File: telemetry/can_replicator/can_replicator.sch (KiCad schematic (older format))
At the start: 33 parts, among them J1 CONN_02X03, U1 MCP2561-E_SN, U2 ATMEGA16M1, U3 USB_MicroB, U4 FT232RL, Y1 Crystal_SMD

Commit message: feat: change to 3 debug LEDs
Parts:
- removed D?: LED_0805, footprints:LED_0805_OEM, symbol formula:LED_0805
- removed R?: R_270K, footprints:R_0805_OEM, symbol formula:R_270K
- gave numbers to parts that had none: 7
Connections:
- net labels removed: DBG4
- wire segments 75 -> 73
- no-connect marks 28 -> 29
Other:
- moved on the sheet: D4, D5, D6

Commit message: fix: change LEDs to 200ohm resistors
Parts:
- removed R4, R5, R6, R7, R8, R9: R_270K, footprints:R_0805_OEM, symbol formula:R_270K
- added R? (x6): R_200K, footprints:R_0805_OEM, symbol formula:R_200K
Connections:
- wire segments 73 -> 76
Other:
- moved on the sheet: D4, D5, D6

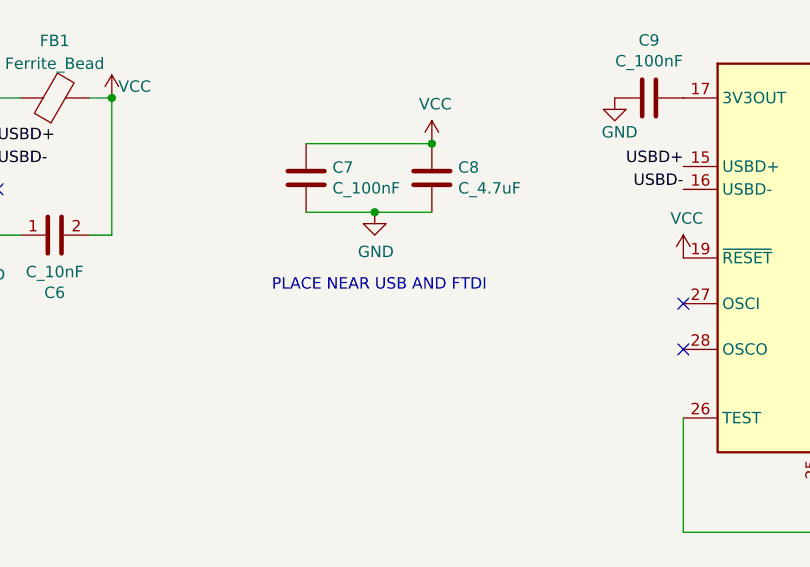
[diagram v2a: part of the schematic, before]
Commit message: docs: update placement of decoupling caps
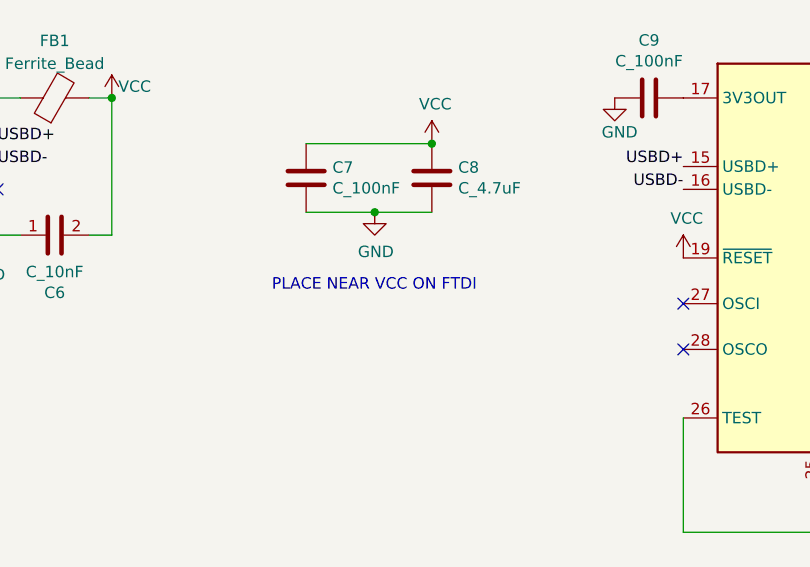
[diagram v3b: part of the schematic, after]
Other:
- note added: "PLACE NEAR VCC ON FTDI"
- note removed: "PLACE NEAR USB AND FTDI"
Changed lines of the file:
@@
 NoConn ~ 3800 1700
 Text Notes 12400 2650 0    50   ~ 0
-PLACE NEAR USB AND FTDI
+PLACE NEAR VCC ON FTDI
 $Comp
 L formula:LED_0805 D4

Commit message: chore: annotate schematic
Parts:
- gave numbers to parts that had none: 6
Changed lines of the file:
@@
 $EndComp
 $Comp
-L power:GND #PWR?
+L power:GND #PWR024
 U 1 1 5FB7CF68
 P 15900 8850
-F 0 "#PWR?" H 15900 8600 50  0001 C CNN
+F 0 "#PWR024" H 15900 8600 50  0001 C CNN
 F 1 "GND" H 15905 8677 50  0000 C CNN
 F 2 "" H 15900 8850 50  0001 C CNN
@@
 NoConn ~ 3800 1600
 $Comp
-L formula:R_200K R?
+L formula:R_200K R7
 U 1 1 5FB83E8C
 P 15750 6750
-F 0 "R?" V 15543 6750 50  0000 C CNN
+F 0 "R7" V 15543 6750 50  0000 C CNN
 F 1 "R_200K" V 15634 6750 50  0000 C CNN
 F 2 "footprints:R_0805_OEM" H 15680 6750 50  0001 C CNN
@@
 $EndComp
 $Comp
-L formula:R_200K R?
+L formula:R_200K R8
 U 1 1 5FB8465B
 P 15750 7150
-F 0 "R?" V 15543 7150 50  0000 C CNN
+F 0 "R8" V 15543 7150 50  0000 C CNN
 F 1 "R_200K" V 15634 7150 50  0000 C CNN
 F 2 "footprints:R_0805_OEM" H 15680 7150 50  0001 C CNN
@@
 $EndComp
 $Comp
-L formula:R_200K R?
+L formula:R_200K R9
 U 1 1 5FB84F88
 P 15750 7500
-F 0 "R?" V 15543 7500 50  0000 C CNN
+F 0 "R9" V 15543 7500 50  0000 C CNN
 F 1 "R_200K" V 15634 7500 50  0000 C CNN
 F 2 "footprints:R_0805_OEM" H 15680 7500 50  0001 C CNN
@@
 $EndComp
 $Comp
-L formula:R_200K R?
+L formula:R_200K R4
 U 1 1 5FB85882
 P 15700 8150
-F 0 "R?" V 15493 8150 50  0000 C CNN
+F 0 "R4" V 15493 8150 50  0000 C CNN
 F 1 "R_200K" V 15584 8150 50  0000 C CNN
 F 2 "footprints:R_0805_OEM" H 15630 8150 50  0001 C CNN
@@
 	15850 8150 15900 8150
 $Comp
-L formula:R_200K R?
+L formula:R_200K R5
 U 1 1 5FB865BA
 P 15700 8500
-F 0 "R?" V 15493 8500 50  0000 C CNN
+F 0 "R5" V 15493 8500 50  0000 C CNN
 F 1 "R_200K" V 15584 8500 50  0000 C CNN
 F 2 "footprints:R_0805_OEM" H 15630 8500 50  0001 C CNN
@@
 	15850 8500 15900 8500
 $Comp
-L formula:R_200K R?
+L formula:R_200K R6
 U 1 1 5FB86F49
 P 15700 8850
-F 0 "R?" V 15493 8850 50  0000 C CNN
+F 0 "R6" V 15493 8850 50  0000 C CNN
 F 1 "R_200K" V 15584 8850 50  0000 C CNN
 F 2 "footprints:R_0805_OEM" H 15630 8850 50  0001 C CNN

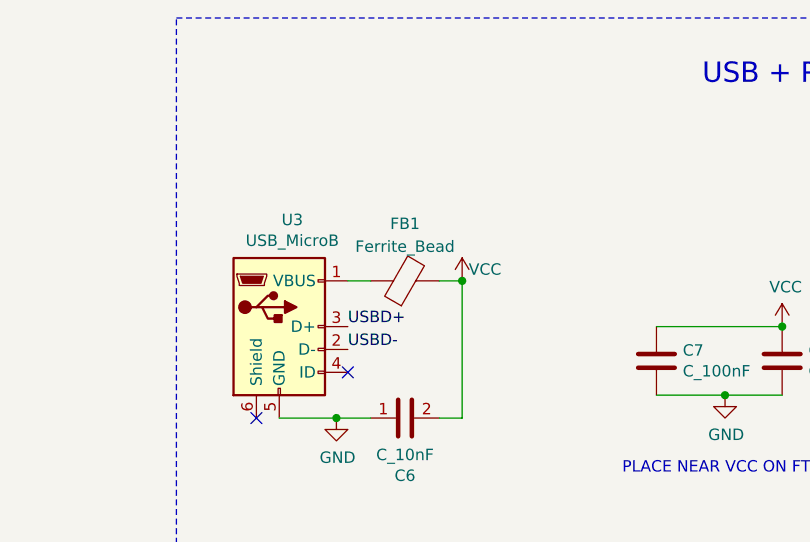
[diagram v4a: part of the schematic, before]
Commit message: feat: remove ferrite bead
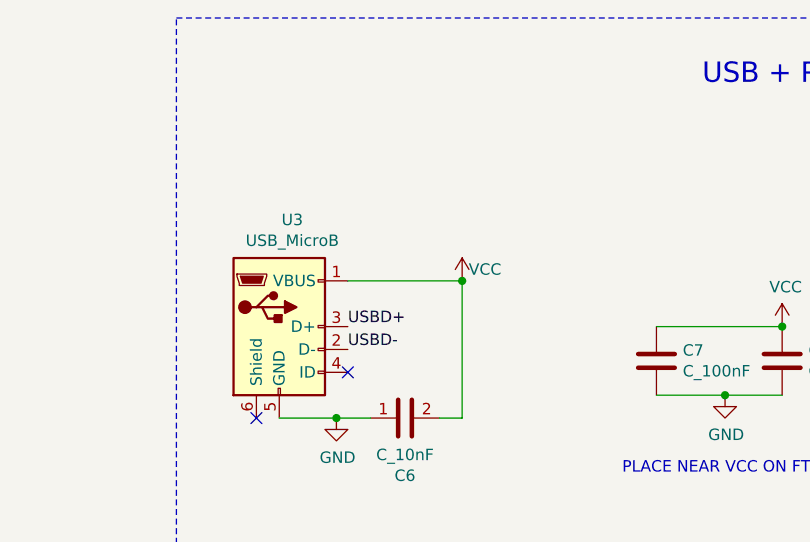
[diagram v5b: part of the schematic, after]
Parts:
- removed FB1: Ferrite_Bead, symbol Device:Ferrite_Bead
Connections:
- net VCC: now also U3.1 (VBUS)
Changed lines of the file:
@@
 Wire Wire Line
 	11300 2400 11150 2400
-Wire Wire Line
-	11200 1800 11300 1800
-$Comp
-L Device:Ferrite_Bead FB1
-U 1 1 5FAF9058
-P 11450 1800
-F 0 "FB1" V 11700 1800 50  0000 C CNN
-F 1 "Ferrite_Bead" V 11600 1800 50  0000 C CNN
-F 2 "" V 11380 1800 50  0001 C CNN
-F 3 "~" H 11450 1800 50  0001 C CNN
-	1    11450 1800
-	0    -1   -1   0
-$EndComp
-Wire Wire Line
-	11600 1800 11700 1800
 Connection ~ 11700 1800
 $Comp
@@
 Wire Wire Line
 	15850 8850 15900 8850
+Wire Wire Line
+	11200 1800 11700 1800
 $EndSCHEMATC

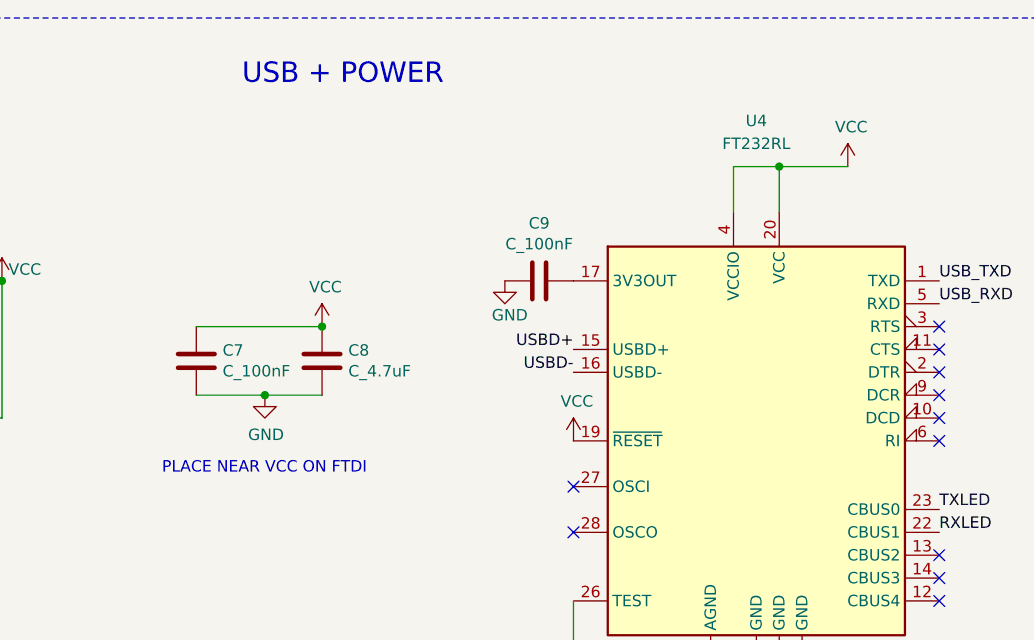
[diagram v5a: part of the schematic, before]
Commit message: style: move decoupling caps near FTDI
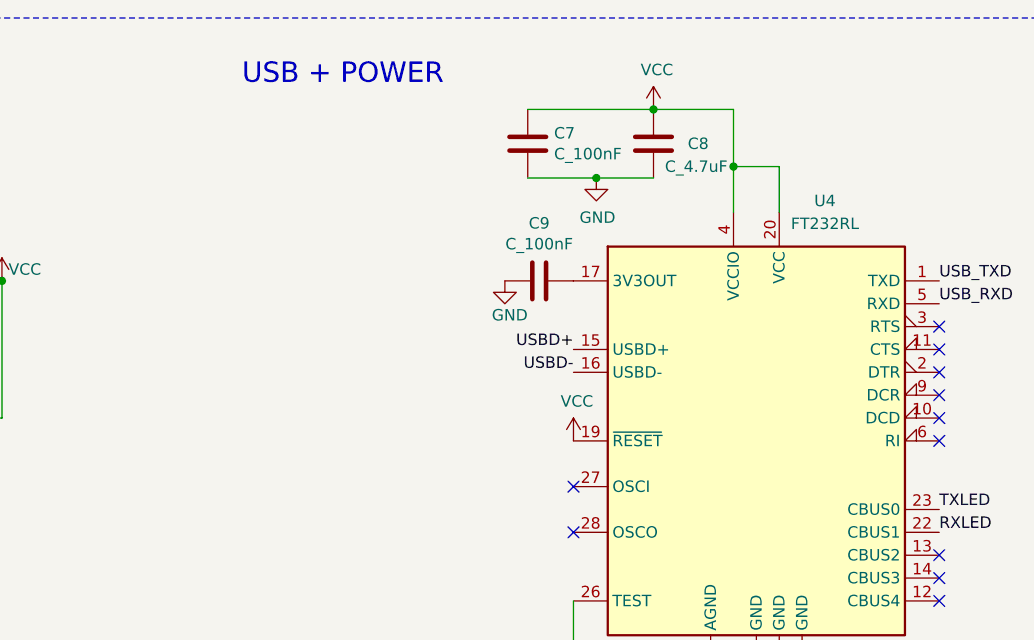
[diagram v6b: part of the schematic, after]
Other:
- note removed: "PLACE NEAR VCC ON FTDI"
- moved on the sheet: C7, C8
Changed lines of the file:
@@
 U 1 1 5FA978AD
 P 15000 2500
-F 0 "U4" H 15000 3900 50  0000 C CNN
-F 1 "FT232RL" H 15000 3800 50  0000 C CNN
+F 0 "U4" H 15300 3550 50  0000 C CNN
+F 1 "FT232RL" H 15300 3450 50  0000 C CNN
 F 2 "Package_SO:SSOP-28_5.3x10.2mm_P0.65mm" H 16100 1600 50  0001 C CNN
 F 3 "https://www.ftdichip.com/Support/Documents/DataSheets/ICs/DS_FT232R.pdf" H 15000 2500 50  0001 C CNN
@@
 Wire Wire Line
 	15100 1500 15100 1300
-Connection ~ 15100 1300
-Wire Wire Line
-	15100 1300 15400 1300
-$Comp
-L power:VCC #PWR0103
-U 1 1 5FADCCAF
-P 15400 1300
-F 0 "#PWR0103" H 15400 1150 50  0001 C CNN
-F 1 "VCC" H 15415 1473 50  0000 C CNN
-F 2 "" H 15400 1300 50  0001 C CNN
-F 3 "" H 15400 1300 50  0001 C CNN
-	1    15400 1300
-	1    0    0    -1
-$EndComp
 Connection ~ 11150 2400
 $Comp
@@
 L power:GND #PWR0107
 U 1 1 5FB2AA73
-P 12850 2300
-F 0 "#PWR0107" H 12850 2050 50  0001 C CNN
-F 1 "GND" H 12855 2127 50  0000 C CNN
-F 2 "" H 12850 2300 50  0001 C CNN
-F 3 "" H 12850 2300 50  0001 C CNN
-	1    12850 2300
-	1    0    0    -1
-$EndComp
-Connection ~ 12850 2300
-Wire Wire Line
-	12850 2300 13100 2300
+P 14300 1350
+F 0 "#PWR0107" H 14300 1100 50  0001 C CNN
+F 1 "GND" H 14305 1177 50  0000 C CNN
+F 2 "" H 14300 1350 50  0001 C CNN
+F 3 "" H 14300 1350 50  0001 C CNN
+	1    14300 1350
+	1    0    0    -1
+$EndComp
+Connection ~ 14300 1350
+Wire Wire Line
+	14300 1350 14550 1350
 $Comp
 L formula:C_100nF C7
 U 1 1 5FB2B96B
-P 12550 2150
-F 0 "C7" H 12665 2196 50  0000 L CNN
-F 1 "C_100nF" H 12665 2105 50  0000 L CNN
-F 2 "footprints:C_0603_1608Metric" H 12588 2000 50  0001 C CNN
-F 3 "http://www.samsungsem.com/kr/support/product-search/mlcc/CL10A475KQ8NNNC.jsp" H 12575 2250 50  0001 C CNN
-F 4 "DK" H 12550 2150 60  0001 C CNN "MFN"
-F 5 "1276-6717-1-ND" H 12550 2150 60  0001 C CNN "MPN"
-F 6 "https://www.digikey.com/product-detail/en/samsung-electro-mechanics/CL10B104KA8WPNC/1276-6717-1-ND/5961576" H 12975 2650 60  0001 C CNN "PurchasingLink"
-	1    12550 2150
-	1    0    0    -1
-$EndComp
-Wire Wire Line
-	12550 2000 13100 2000
+P 14000 1200
+F 0 "C7" H 14115 1246 50  0000 L CNN
+F 1 "C_100nF" H 14115 1155 50  0000 L CNN
+F 2 "footprints:C_0603_1608Metric" H 14038 1050 50  0001 C CNN
+F 3 "http://www.samsungsem.com/kr/support/product-search/mlcc/CL10A475KQ8NNNC.jsp" H 14025 1300 50  0001 C CNN
+F 4 "DK" H 14000 1200 60  0001 C CNN "MFN"
+F 5 "1276-6717-1-ND" H 14000 1200 60  0001 C CNN "MPN"
+F 6 "https://www.digikey.com/product-detail/en/samsung-electro-mechanics/CL10B104KA8WPNC/1276-6717-1-ND/5961576" H 14425 1700 60  0001 C CNN "PurchasingLink"
+	1    14000 1200
+	1    0    0    -1
+$EndComp
+Wire Wire Line
+	14000 1050 14550 1050
 $Comp
 L formula:C_4.7uF C8
 U 1 1 5FB2C8CC
-P 13100 2150
-F 0 "C8" H 13215 2196 50  0000 L CNN
-F 1 "C_4.7uF" H 13215 2105 50  0000 L CNN
-F 2 "footprints:C_0603_1608Metric" H 13138 2000 50  0001 C CNN
-F 3 "http://www.samsungsem.com/kr/support/product-search/mlcc/CL10A475KQ8NNNC.jsp" H 13125 2250 50  0001 C CNN
-F 4 "DK" H 13100 2150 60  0001 C CNN "MFN"
-F 5 "1276-1045-1-ND" H 13100 2150 60  0001 C CNN "MPN"
-F 6 "https://www.digikey.com/product-detail/en/samsung-electro-mechanics/CL10A475KQ8NNNC/1276-1045-1-ND/3889131" H 13525 2650 60  0001 C CNN "PurchasingLink"
-	1    13100 2150
-	1    0    0    -1
-$EndComp
-Wire Wire Line
-	12550 2300 12850 2300
+P 14550 1200
+F 0 "C8" H 14700 1200 50  0000 L CNN
+F 1 "C_4.7uF" H 14600 1100 50  0000 L CNN
+F 2 "footprints:C_0603_1608Metric" H 14588 1050 50  0001 C CNN
+F 3 "http://www.samsungsem.com/kr/support/product-search/mlcc/CL10A475KQ8NNNC.jsp" H 14575 1300 50  0001 C CNN
+F 4 "DK" H 14550 1200 60  0001 C CNN "MFN"
+F 5 "1276-1045-1-ND" H 14550 1200 60  0001 C CNN "MPN"
+F 6 "https://www.digikey.com/product-detail/en/samsung-electro-mechanics/CL10A475KQ8NNNC/1276-1045-1-ND/3889131" H 14975 1700 60  0001 C CNN "PurchasingLink"
+	1    14550 1200
+	1    0    0    -1
+$EndComp
+Wire Wire Line
+	14000 1350 14300 1350
 $Comp
 L formula:LED_0805 D3
@@
 L power:VCC #PWR020
 U 1 1 5FB37814
-P 13100 2000
-F 0 "#PWR020" H 13100 1850 50  0001 C CNN
-F 1 "VCC" H 13115 2173 50  0000 C CNN
-F 2 "" H 13100 2000 50  0001 C CNN
-F 3 "" H 13100 2000 50  0001 C CNN
-	1    13100 2000
-	1    0    0    -1
-$EndComp
-Connection ~ 13100 2000
+P 14550 1050
+F 0 "#PWR020" H 14550 900 50  0001 C CNN
+F 1 "VCC" H 14565 1223 50  0000 C CNN
+F 2 "" H 14550 1050 50  0001 C CNN
+F 3 "" H 14550 1050 50  0001 C CNN
+	1    14550 1050
+	1    0    0    -1
+$EndComp
+Connection ~ 14550 1050
 $Comp
 L power:GND #PWR023
@@
 NoConn ~ 3800 2000
 NoConn ~ 3800 1700
-Text Notes 12400 2650 0    50   ~ 0
-PLACE NEAR VCC ON FTDI
 $Comp
 L formula:LED_0805 D4
@@
 Wire Wire Line
 	11200 1800 11700 1800
+Wire Wire Line
+	14550 1050 14900 1050
+Wire Wire Line
+	14900 1050 14900 1300
+Connection ~ 14900 1300
 $EndSCHEMATC

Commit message: fix: misc. fixes based on design checklist
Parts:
- removed R4, R5, R6, R7, R8, R9: R_200K, footprints:R_0805_OEM, symbol formula:R_200K
- added J2: MM_M_VT_20, footprints:micromatch_female_vert_20, symbol formula:MM_M_VT_20
- added R4, R5, R6, R7, R8, R9: R_200, footprints:R_0805_OEM, symbol formula:R_200
- added TP1, TP2: TP, footprints:tp_1.6mm, symbol formula:TP
- U3: footprint Connectors_USB:USB_Micro-B_Molex-105017-0001 -> Connector_USB:USB_Micro-B_Molex-105017-0001
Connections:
- net GND: now also J2.1, J2.10, J2.11, J2.12, J2.13, J2.14, J2.15, J2.16, J2.17, J2.18, J2.19, J2.20, J2.5, J2.6, J2.7, J2.8, J2.9, R4.1, R5.1, R6.1, R9.1, TP1.1 (TP)
- net RXLED: now also R7.1
- net TXLED: now also R8.1
- net VCC: now also TP2.1 (TP)
- net at D3.1 (K): now also R9.2
- net at D4.1 (K): now also R4.2
- net at D2.1 (K): now also R8.2
- net at D1.1 (K): now also R7.2
- net at D5.1 (K): now also R5.2
- net at D6.1 (K): now also R6.2
- net CAN_HI renamed CAN_+
- net CAN_+: now also J2.3
- net CAN_LO renamed CAN_-
- net CAN_-: now also J2.4
- no-connect marks 29 -> 30
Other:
- moved on the sheet: C1, C2, C3, C4, C5, C6, C7, C8, C9, D1, D2, D3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

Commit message: fix: begin removal of template-rescue
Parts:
- added D?: D_Zener_5.6V, footprints:D_5.6V_Zener, symbol formula:D_Zener_5.6V
- U2: symbol template-rescue:ATMEGA16M1-formula -> formula:ATMEGA16M1
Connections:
- net GND: now also D?.2 (A)
- net VCC: now also D?.1 (K)
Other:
- note removed: "POWER FLAGS\n"
- moved on the sheet: C6
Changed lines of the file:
@@
 Comment4 ""
 $EndDescr
-$Comp
-L power:GND #PWR0108
-U 1 1 5BEE3CCE
-P 15300 2800
-F 0 "#PWR0108" H 15300 2550 50  0001 C CNN
-F 1 "GND" H 15305 2627 50  0000 C CNN
-F 2 "" H 15300 2800 50  0001 C CNN
-F 3 "" H 15300 2800 50  0001 C CNN
-	1    15300 2800
-	1    0    0    -1
-$EndComp
 Text Label 3950 2550 0    50   ~ 0
 CAN_TX
@@
 Text Notes 3850 5350 0    89   ~ 0
 16 MHz CRYSTAL\n
-Text Notes 14900 2350 0    89   ~ 0
-POWER FLAGS\n
-$Comp
-L power:PWR_FLAG #FLG02
-U 1 1 5D615167
-P 14900 2650
-F 0 "#FLG02" H 14900 2725 50  0001 C CNN
-F 1 "PWR_FLAG" H 14900 2824 50  0000 C CNN
-F 2 "" H 14900 2650 50  0001 C CNN
-F 3 "~" H 14900 2650 50  0001 C CNN
-	1    14900 2650
-	1    0    0    -1
-$EndComp
-$Comp
-L power:PWR_FLAG #FLG03
-U 1 1 5D615217
-P 15300 2650
-F 0 "#FLG03" H 15300 2725 50  0001 C CNN
-F 1 "PWR_FLAG" H 15300 2824 50  0000 C CNN
-F 2 "" H 15300 2650 50  0001 C CNN
-F 3 "~" H 15300 2650 50  0001 C CNN
-	1    15300 2650
-	1    0    0    -1
-$EndComp
-$Comp
-L power:VCC #PWR016
-U 1 1 5D6181B6
-P 14900 2800
-F 0 "#PWR016" H 14900 2650 50  0001 C CNN
-F 1 "VCC" H 14918 2973 50  0000 C CNN
-F 2 "" H 14900 2800 50  0001 C CNN
-F 3 "" H 14900 2800 50  0001 C CNN
-	1    14900 2800
-	-1   0    0    1
-$EndComp
-$Comp
-L power:GND #PWR017
-U 1 1 5D622997
-P 15600 2800
-F 0 "#PWR017" H 15600 2550 50  0001 C CNN
-F 1 "GND" H 15605 2627 50  0000 C CNN
-F 2 "" H 15600 2800 50  0001 C CNN
-F 3 "" H 15600 2800 50  0001 C CNN
-	1    15600 2800
-	1    0    0    -1
-$EndComp
-Text Label 15600 2650 2    50   ~ 0
-GND
 $Comp
 L template-rescue:CONN_02X03-formula J1
@@
 Wire Wire Line
 	6950 2400 6950 2450
-Wire Wire Line
-	14900 2650 14900 2800
-Wire Wire Line
-	15300 2650 15300 2800
-Wire Wire Line
-	15600 2650 15600 2800
 Wire Wire Line
 	6850 2400 6950 2400
@@
 	1    0    0    -1
 $EndComp
-Wire Wire Line
-	2000 7550 2000 6950
-Wire Wire Line
-	2000 7550 1900 7550
 $Comp
 L formula:C_10nF C6
 U 1 1 5FAF39CA
-P 1750 7550
-F 0 "C6" V 1498 7550 50  0000 C CNN
-F 1 "C_10nF" V 1589 7550 50  0000 C CNN
-F 2 "footprints:C_0805_OEM" H 1550 7550 50  0001 C CNN
-F 3 "http://www.samsungsem.com/kr/support/product-search/mlcc/__icsFiles/afieldfile/2018/07/23/CL21B103KBANNNC.pdf" H 1650 7650 50  0001 C CNN
-F 4 "DK" H 1750 7750 50  0001 C CNN "MFN"
-F 5 "1276-1015-1-ND" H 1850 7850 50  0001 C CNN "MPN"
-F 6 "https://www.digikey.com/product-detail/en/samsung-electro-mechanics/CL21B103KBANNNC/1276-1015-1-ND/3889101" H 1950 7950 50  0001 C CNN "PurchasingLink"
-	1    1750 7550
+P 2100 7550
+F 0 "C6" V 1848 7550 50  0000 C CNN
+F 1 "C_10nF" V 1939 7550 50  0000 C CNN
+F 2 "footprints:C_0805_OEM" H 1900 7550 50  0001 C CNN
+F 3 "http://www.samsungsem.com/kr/support/product-search/mlcc/__icsFiles/afieldfile/2018/07/23/CL21B103KBANNNC.pdf" H 2000 7650 50  0001 C CNN
+F 4 "DK" H 2100 7750 50  0001 C CNN "MFN"
+F 5 "1276-1015-1-ND" H 2200 7850 50  0001 C CNN "MPN"
+F 6 "https://www.digikey.com/product-detail/en/samsung-electro-mechanics/CL21B103KBANNNC/1276-1015-1-ND/3889101" H 2300 7950 50  0001 C CNN "PurchasingLink"
+	1    2100 7550
 	0    -1   -1   0
 $EndComp
-Wire Wire Line
-	1600 7550 1500 7550
-Connection ~ 2000 6950
 $Comp
 L power:GND #PWR0107
@@
 	14950 6000 15100 6000
 $Comp
-L template-rescue:ATMEGA16M1-formula U2
+L formula:ATMEGA16M1 U2
 U 1 1 5D58A7A6
 P 2850 3150
@@
 Wire Notes Line
 	14100 3400 16000 3400
-Wire Notes Line
-	16000 2150 16000 3100
-Wire Notes Line
-	16000 3100 14150 3100
-Wire Notes Line
-	14150 3100 14150 2150
 Wire Notes Line
 	16000 1000 16000 1850
@@
 $EndComp
 Wire Notes Line
-	14150 2150 16000 2150
-Wire Notes Line
 	5100 5800 5100 9200
 Wire Notes Line
@@
 Connection ~ 1700 6950
 Wire Wire Line
-	1700 6950 2000 6950
+	1700 6950 1900 6950
 $Comp
 L formula:TP TP1
@@
 $EndComp
 Connection ~ 1300 7550
-Connection ~ 1500 7550
 Wire Wire Line
 	1300 7550 1500 7550
@@
 	14600 8550 15000 8550
 $Comp
-L power:GND #PWR?
+L power:GND #PWR0103
 U 1 1 5FD1E507
 P 14600 8550
-F 0 "#PWR?" H 14600 8300 50  0001 C CNN
+F 0 "#PWR0103" H 14600 8300 50  0001 C CNN
 F 1 "GND" H 14605 8377 50  0000 C CNN
 F 2 "" H 14600 8550 50  0001 C CNN
@@
 	1    0    0    -1
 $EndComp
+$Comp
+L formula:D_Zener_5.6V D?
+U 1 1 5FD3EFD3
+P 1900 7250
+F 0 "D?" V 1854 7329 50  0000 L CNN
+F 1 "D_Zener_5.6V" V 1945 7329 50  0000 L CNN
+F 2 "footprints:D_5.6V_Zener" H 1800 7250 50  0001 C CNN
+F 3 "https://www.mccsemi.com/pdf/Products/3SMBJ5918B-3SMBJ5956B(DO-214AA).pdf" H 1900 7350 50  0001 C CNN
+F 4 "DK" H 2100 7550 60  0001 C CNN "MFN"
+F 5 "3SMBJ5919B-TP" H 2000 7450 60  0001 C CNN "MPN"
+F 6 "https://www.digikey.com/en/products/detail/micro-commercial-co/3SMBJ5919B-TP/8554648" H 2300 7750 60  0001 C CNN "PurchasingLink"
+	1    1900 7250
+	0    1    1    0
+$EndComp
+Wire Wire Line
+	1900 7100 1900 6950
+Connection ~ 1900 6950
+Wire Wire Line
+	1900 6950 2000 6950
+Wire Wire Line
+	1900 7400 1900 7550
+Connection ~ 1900 7550
+Connection ~ 1500 7550
+Wire Wire Line
+	1500 7550 1900 7550
+Wire Wire Line
+	1950 7550 1900 7550
+Wire Wire Line
+	2500 7550 2500 6950
+Wire Wire Line
+	2500 6950 2000 6950
+Connection ~ 2000 6950
+Wire Wire Line
+	2250 7550 2500 7550
 $EndSCHEMATC
